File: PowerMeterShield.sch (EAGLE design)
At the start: 18 parts, among them IC1 MCP3426A0-E/SN, IC2 INA138, IC3 ADUM1250ARZ

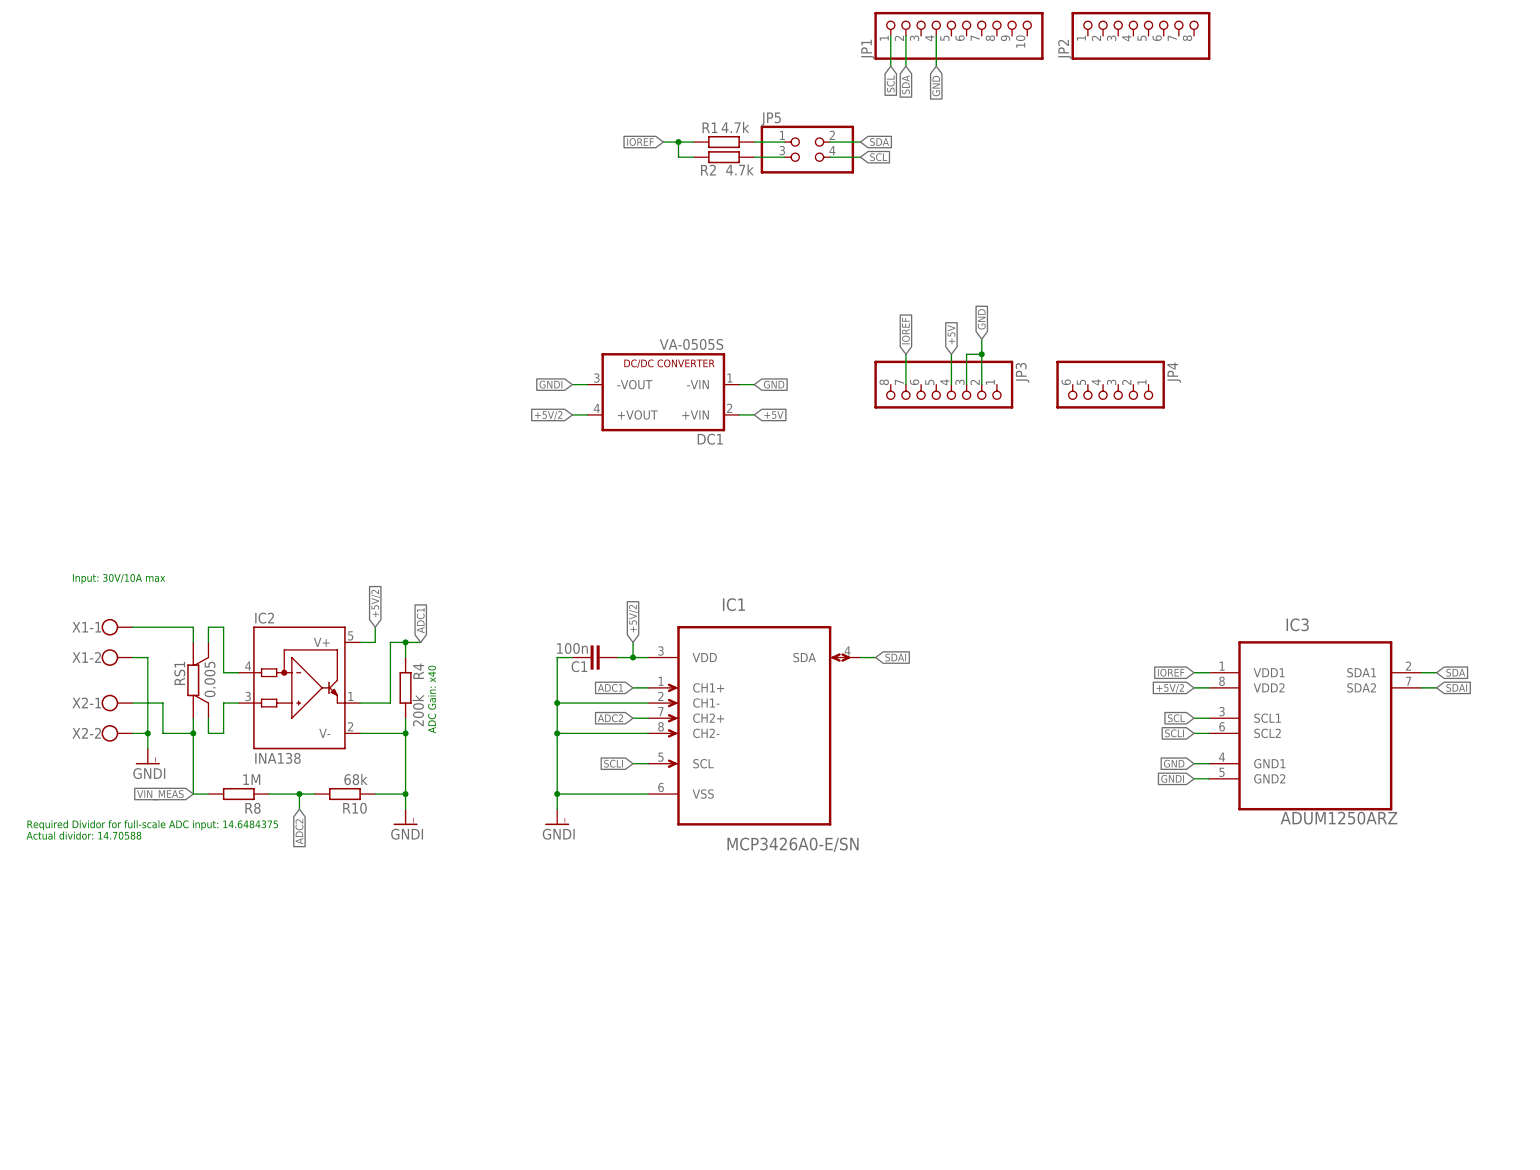
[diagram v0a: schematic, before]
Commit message: Updated to a modified design for differential voltage measurement
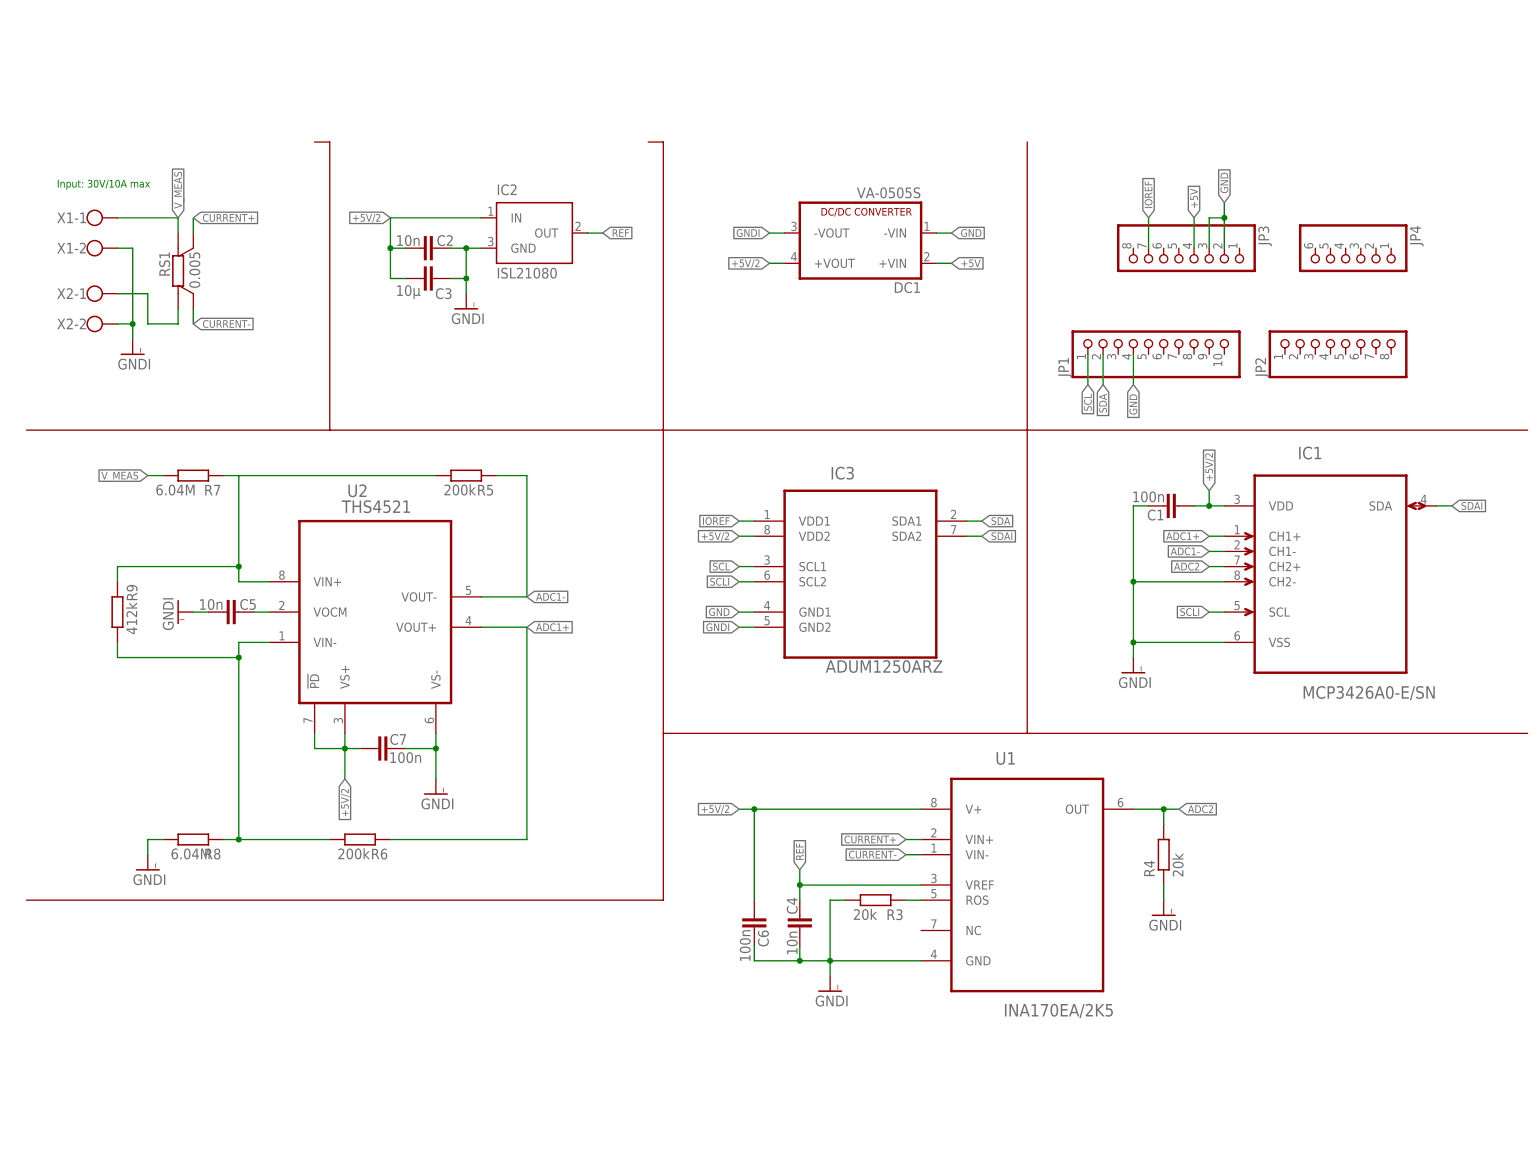
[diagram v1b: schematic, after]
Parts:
- removed JP5: (no value), pinhead:PINHD-2X2
- removed R1, R2: 4.7k, rcl:R-EU_R0805
- removed R10: 68k, rcl:R-EU_R0805
- added C2, C4, C5: 10n, rcl:C-EUC0805
- added C3: 10µ, rcl:C-EUC0805
- added C6, C7: 100n, rcl:C-EUC0805
- added R3: 20k, rcl:R-EU_R0805
- added R5, R6: 200k, rcl:R-EU_R0805
- added R7: 6.04M, rcl:R-EU_R0805
- added R9: 412k, rcl:R-EU_R0805
- added U1: INA170EA/2K5, INA170:INA170EA/2K5
- added U2: THS4521, THS4531:THS4531AID
- IC2: value INA138 -> ISL21080; device burr-brown:INA138 -> maxim:MAX6520; OC_DIGIKEY INA168NADKR-ND -> (none); OC_FARNELL 1206900RL -> (none); PRICE_10 1.21 -> (none)
- JP1: OC_ELECTRODRAGON (none) -> CCO3507; PRICE_10 (none) -> 0.16; PRICE_100 (none) -> 0.16
- JP2, JP3: OC_ELECTRODRAGON (none) -> CCO3509; PRICE_10 (none) -> 0.12; PRICE_100 (none) -> 0.12
- JP4: OC_ELECTRODRAGON (none) -> CCO3510; PRICE_10 (none) -> 0.12; PRICE_100 (none) -> 0.12
- R4: value 200k -> 20k; OC_FARNELL 2129299 -> (none); PRICE_100 0.001 -> (none)
- R8: value 1M -> 6.04M; OC_FARNELL 2129354 -> (none); PRICE_100 0.001 -> (none)
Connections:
- removed net ADC1: IC1.CH1+, IC2.OUT, R4.2
- removed net N$3: JP5.1, R1.2
- removed net N$4: JP5.3, R2.2
- removed net N$5: RS1.I2, X1-1.KL
- new net ADC1+: IC1.CH1+, R6.2, U2.VOUT+
- new net ADC1-: IC1.CH1-, R5.2, U2.VOUT-
- new net CURRENT+: RS1.S2, U1.VIN+
- new net CURRENT-: RS1.S1, U1.VIN-
- new net N$10: R6.1, R8.2, R9.1, U2.VIN-
- new net N$7: R3.2, U1.ROS
- new net REF: C4.2, IC2.OUT, U1.VREF
- new net V_MEAS: R7.1, RS1.I2, X1-1.KL
- net +5V/2: now also C2.1, C3.1, C6.1, C7.1, IC2.IN, U1.V+, U2.!PD, U2.VS+; no longer IC2.V+
- net ADC2: now also R4.2, U1.OUT; no longer R10.2, R8.1
- net GNDI: now also C2.2, C3.2, C4.1, C5.1, C6.2, C7.2, IC2.GND, R3.1, R8.1, U1.GND, U2.VS-; no longer IC1.CH1-, IC2.V-, R10.1
- net IOREF: no longer R1.1, R2.1
- net N$1: now also C5.2, U2.VOCM; no longer IC2.IN+, RS1.S1
- net N$2: now also R5.1, R7.2, R9.2, U2.VIN+; no longer IC2.IN-, RS1.S2
- net SCL: no longer JP5.4
- net SDA: no longer JP5.2
- net VIN_MEAS: no longer R8.2
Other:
- note removed: "ADC Gain: x40"
- note removed: "Required Dividor for full-scale ADC input: 14.6484375 Actual dividor: 14.70588"
- moved on the sheet: C1, DC1, IC1, IC3, JP1, JP2, JP3, JP4, R4, R8, RS1, X1-1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

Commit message: Added domain name + descriptions for the functional schematic blocks
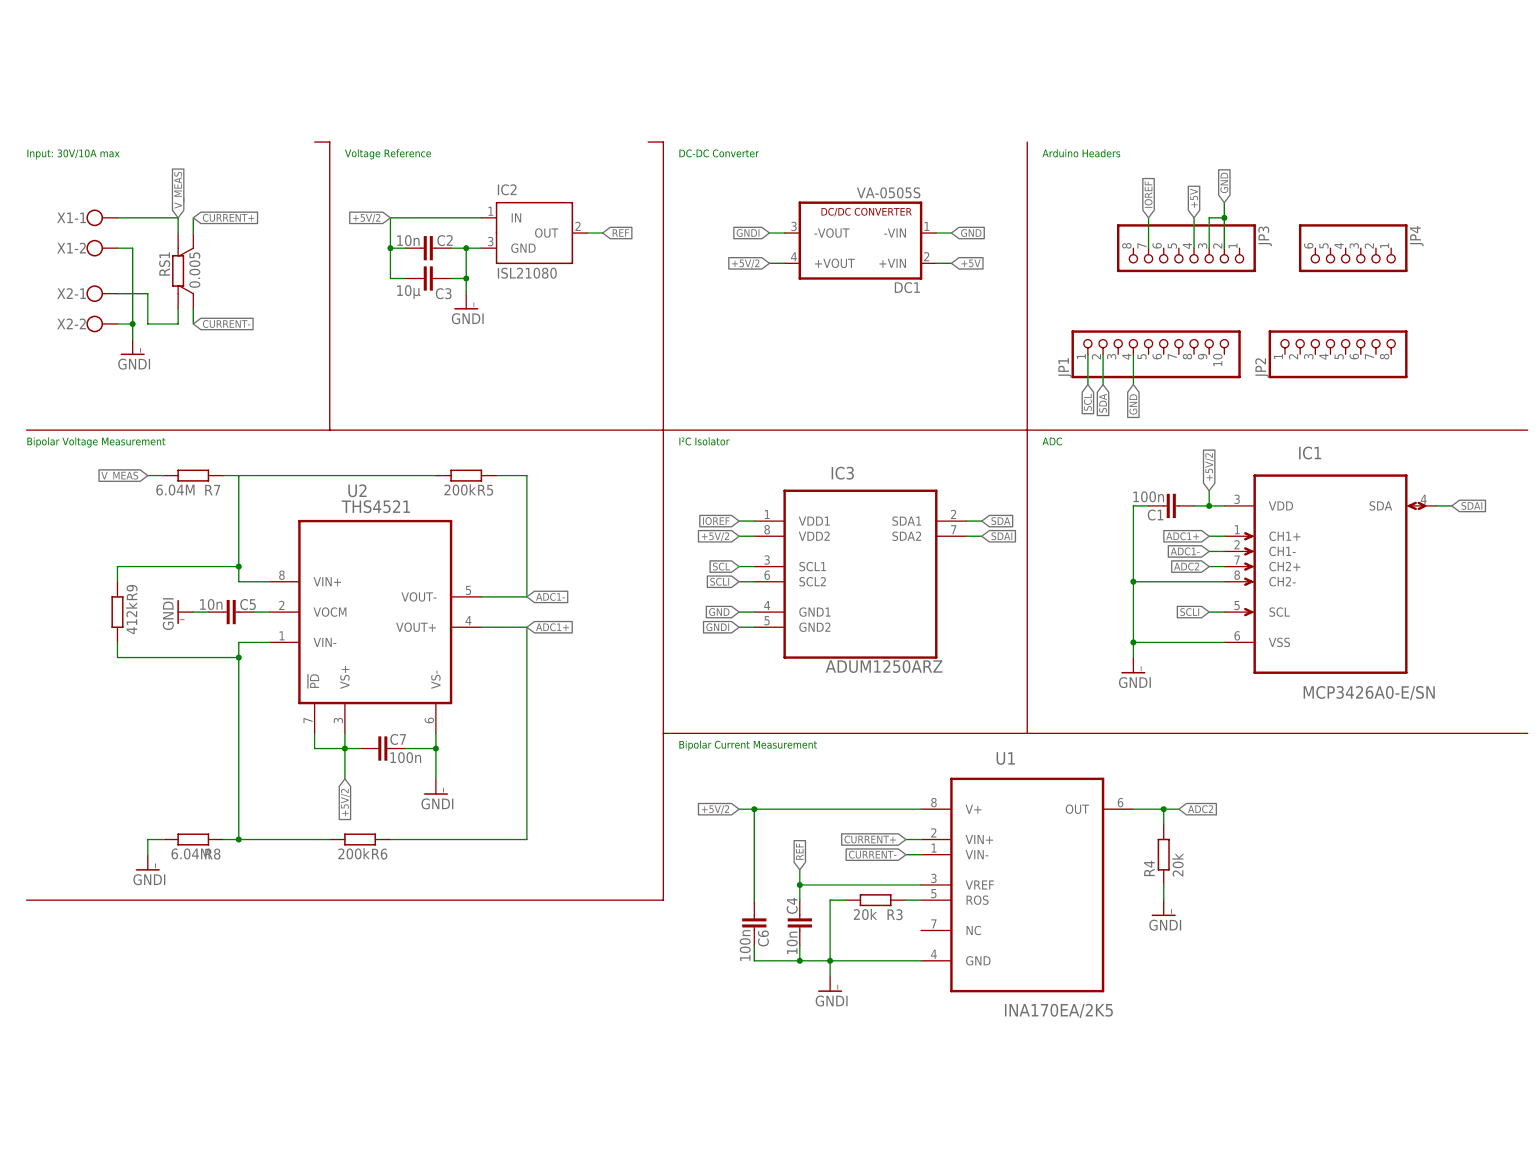
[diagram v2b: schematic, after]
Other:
- note added: "ADC"
- note added: "Arduino Headers"
- note added: "Bipolar Current Measurement"
- note added: "Bipolar Voltage Measurement"
- note added: "DC-DC Converter"
- note added: "I²C Isolator"
- note added: "Voltage Reference"
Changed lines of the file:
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@@
 <sheet>
 <plain>
-<text x="10.16" y="167.64" size="1.27" layer="91">Input: 30V/10A max</text>
+<text x="5.08" y="172.72" size="1.27" layer="91">Input: 30V/10A max</text>
 <wire x1="5.08" y1="127" x2="55.88" y2="127" width="0.1524" layer="94"/>
 <wire x1="55.88" y1="127" x2="111.76" y2="127" width="0.1524" layer="94"/>
@@
 <wire x1="111.76" y1="76.2" x2="111.76" y2="48.26" width="0.1524" layer="94"/>
 <wire x1="111.76" y1="48.26" x2="5.08" y2="48.26" width="0.1524" layer="94"/>
+<text x="58.42" y="172.72" size="1.27" layer="91">Voltage Reference</text>
+<text x="114.3" y="172.72" size="1.27" layer="91">DC-DC Converter</text>
+<text x="175.26" y="172.72" size="1.27" layer="91">Arduino Headers</text>
+<text x="175.26" y="124.46" size="1.27" layer="91">ADC</text>
+<text x="114.3" y="124.46" size="1.27" layer="91">I²C Isolator</text>
+<text x="5.08" y="124.46" size="1.27" layer="91">Bipolar Voltage Measurement</text>
+<text x="114.3" y="73.66" size="1.27" layer="91">Bipolar Current Measurement</text>
 </plain>
 <instances>

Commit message: Added non-isolated variant
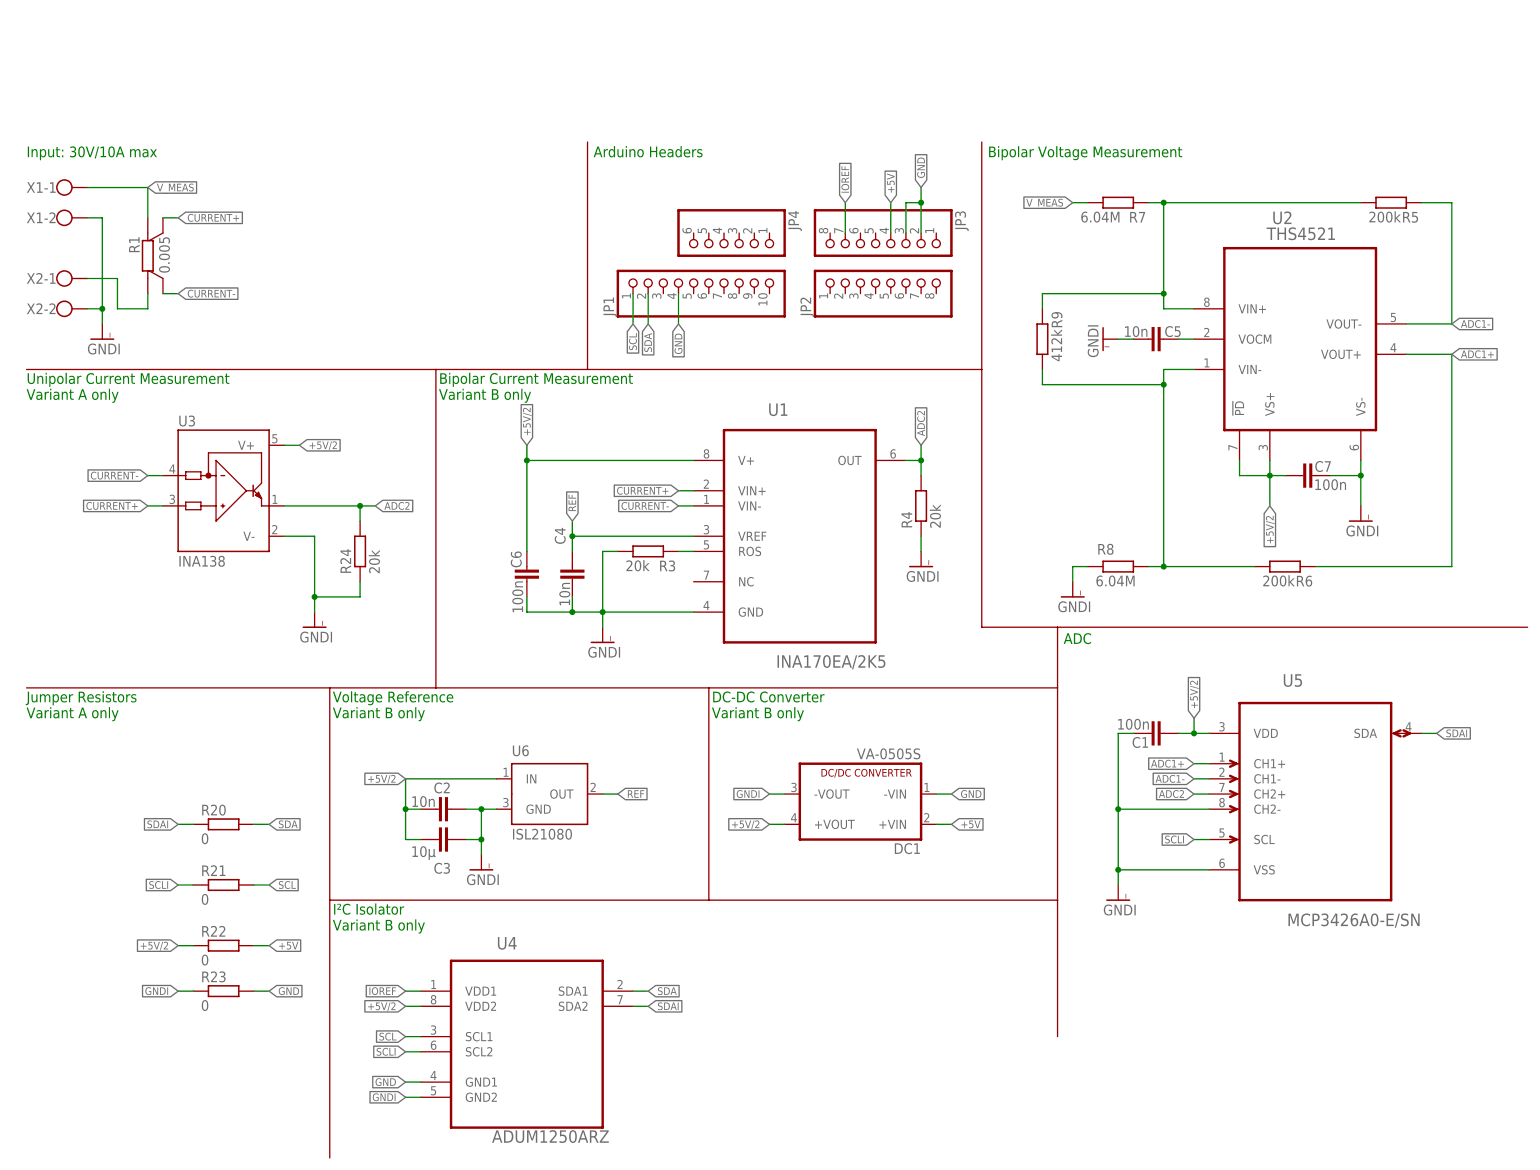
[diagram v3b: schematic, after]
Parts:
- removed IC1: MCP3426A0-E/SN, MCP3428:MCP3426A0-E/SN
- removed IC2: ISL21080, maxim:MAX6520
- removed IC3: ADUM1250ARZ, Adum1250:ADUM1250ARZ
- removed RS1: 0.005, R-Vishay:SHUNT-4CSM3675M
- added R1: 0.005, R-Vishay:SHUNT-4CSM3675M
- added R20, R21, R22, R23: 0, rcl:R-EU_R2010
- added R24: 20k, rcl:R-EU_R0805
- added U3: INA138, burr-brown:INA138
- added U4: ADUM1250ARZ, Adum1250:ADUM1250ARZ
- added U5: MCP3426A0-E/SN, MCP3428:MCP3426A0-E/SN
- added U6: ISL21080, maxim:MAX6520
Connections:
- net +5V: now also R22.2
- net +5V/2: now also R22.1, U3.V+, U4.VDD2, U5.VDD, U6.IN; no longer IC1.VDD, IC2.IN, IC3.VDD2
- net ADC1+: now also U5.CH1+; no longer IC1.CH1+
- net ADC1-: now also U5.CH1-; no longer IC1.CH1-
- net ADC2: now also R24.2, U3.OUT, U5.CH2+; no longer IC1.CH2+
- net CURRENT+: now also R1.S2, U3.IN+; no longer RS1.S2
- net CURRENT-: now also R1.S1, U3.IN-; no longer RS1.S1
- net GND: now also R23.2, U4.GND1; no longer IC3.GND1
- net GNDI: now also R23.1, R24.1, U3.V-, U4.GND2, U5.CH2-, U5.VSS, U6.GND; no longer IC1.CH2-, IC1.VSS, IC2.GND, IC3.GND2
- net IOREF: now also U4.VDD1; no longer IC3.VDD1
- net REF: now also U6.OUT; no longer IC2.OUT
- net SCL: now also R21.2, U4.SCL1; no longer IC3.SCL1
- net SCLI: now also R21.1, U4.SCL2, U5.SCL; no longer IC1.SCL, IC3.SCL2
- net SDA: now also R20.2, U4.SDA1; no longer IC3.SDA1
- net SDAI: now also R20.1, U4.SDA2, U5.SDA; no longer IC1.SDA, IC3.SDA2
- net VIN_MEAS: now also R1.I1; no longer RS1.I1
- net V_MEAS: now also R1.I2; no longer RS1.I2
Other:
- note added: "Bipolar Current Measurement Variant B only"
- note added: "DC-DC Converter Variant B only"
- note added: "I²C Isolator Variant B only"
- note added: "Jumper Resistors Variant A only"
- note added: "Unipolar Current Measurement Variant A only"
- note added: "Voltage Reference Variant B only"
- note removed: "Bipolar Current Measurement"
- note removed: "DC-DC Converter"
- note removed: "I²C Isolator"
- note removed: "Voltage Reference"
- moved on the sheet: C1, C2, C3, C4, C5, C6, C7, DC1, JP1, JP2, JP3, JP4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
